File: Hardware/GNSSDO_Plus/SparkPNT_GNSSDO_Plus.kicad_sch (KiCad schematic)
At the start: 51 parts, among them J7 Qwiic_Vertical, J9 Screw_Cage_3.5mm-10, U1 ESP32-WROVER-IE-N16R8

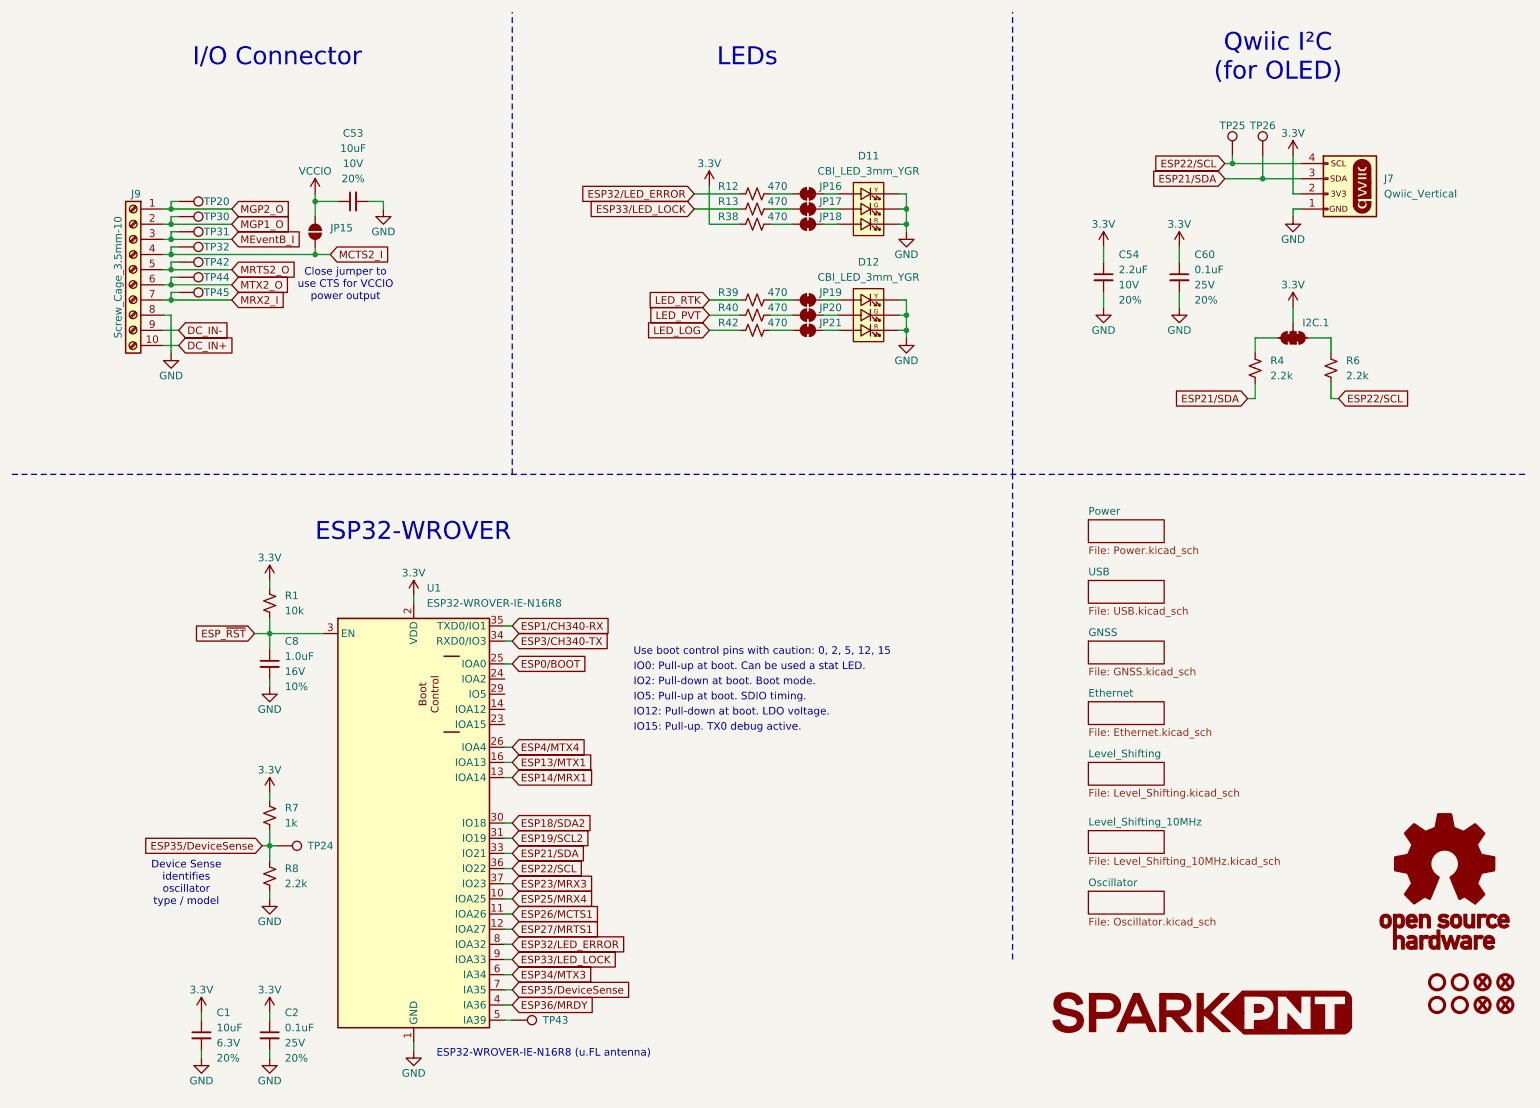
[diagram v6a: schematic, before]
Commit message: GNSSDO+ v02 PCB - with DP5305 PoE module, PowerPath Controllers and MS8607 PHT sensor
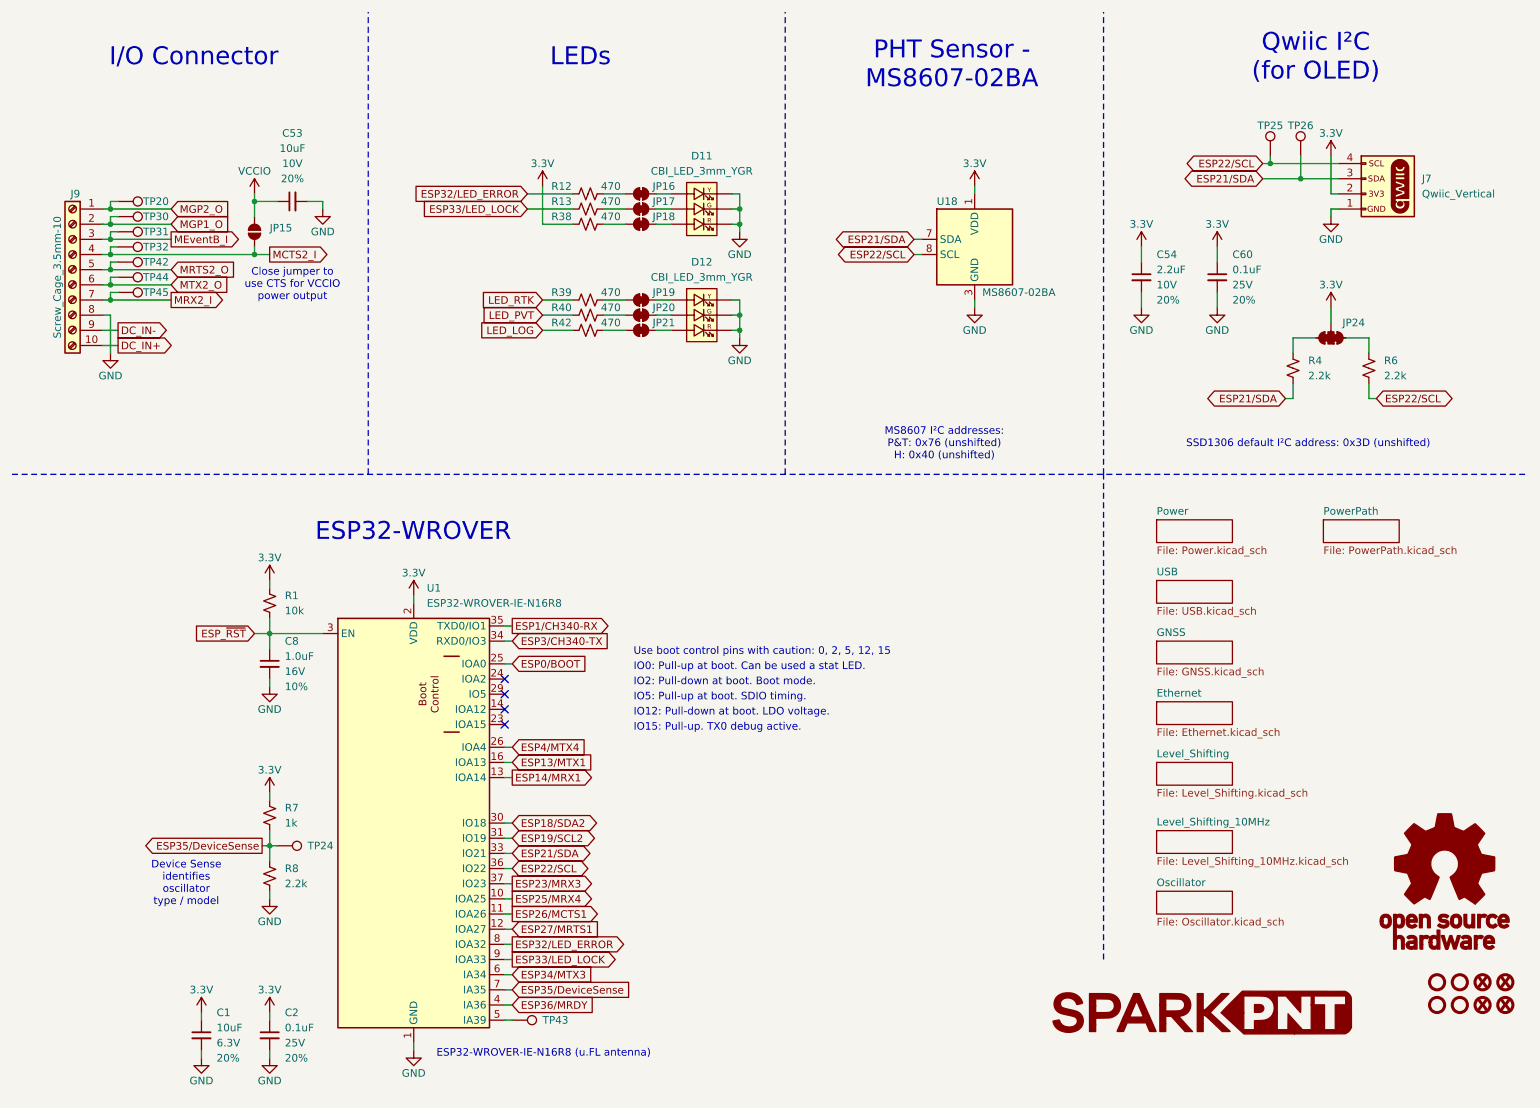
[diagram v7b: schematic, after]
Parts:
- added U18: MS8607-02BA, SparkFun-Semiconductor-Standard:LGA-8_3x5mm_P1.25mm, symbol SparkFun-Sensor:MS8607-02BA
- J7: footprint SparkFun-Connector:JST_SMD_1.0mm-4_Vertical -> SparkFun-Connector:JST_SMD_1.0mm-4_Vertical_Black
- renumbered I2C.1 to JP24
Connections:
- net 3.3V: now also U18.1 (VDD)
- net ESP21/SDA: now also U18.7 (SDA)
- net ESP22/SCL: now also U18.8 (SCL)
- net GND: now also U18.3 (GND)
- no-connect marks 0 -> 4
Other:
- added sheet PowerPath (PowerPath.kicad_sch)
- note added: "MS8607 I²C addresses: P&T: 0x76 (unshifted) H: 0x40 (unshifted)"
- note added: "PHT Sensor - MS8607-02BA"
- note added: "SSD1306 default I²C address: 0x3D (unshifted)"
- company: (none) -> SparkFun Electronics
- moved on the sheet: C53, C54, C60, D11, D12, J7, J9, JP15, JP16, JP17, JP18, JP19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
